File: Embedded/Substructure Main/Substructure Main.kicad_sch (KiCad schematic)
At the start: 30 parts, among them J1 M Pins, J2 C Pins, U1 G0 FFC, U2 G1 FFC, U3 S FFC, U4 USB2513B_Bi, U5 MCP7940N-xMNY, U6 INA220AIDGSR

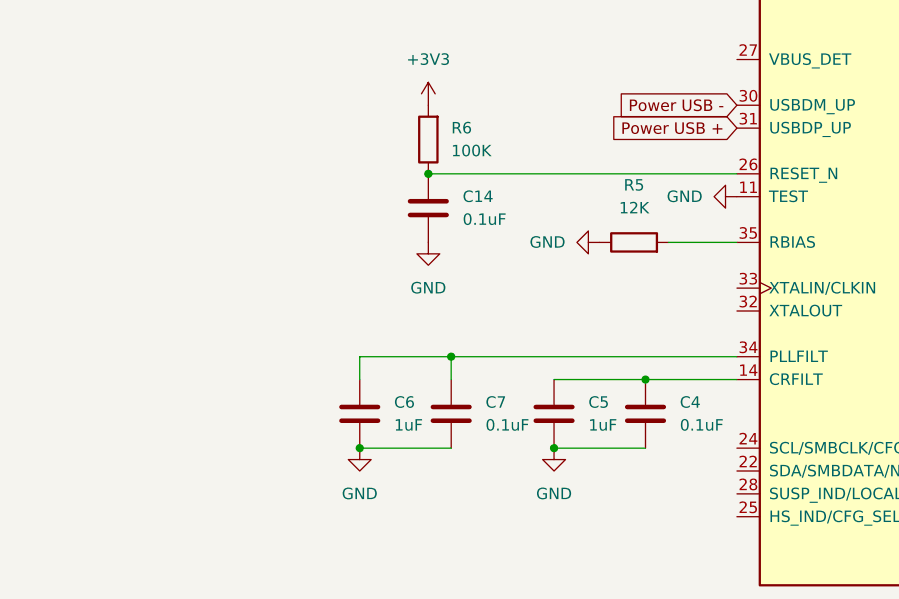
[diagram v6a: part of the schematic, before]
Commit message: Added Crystal to USB2513B_Bi
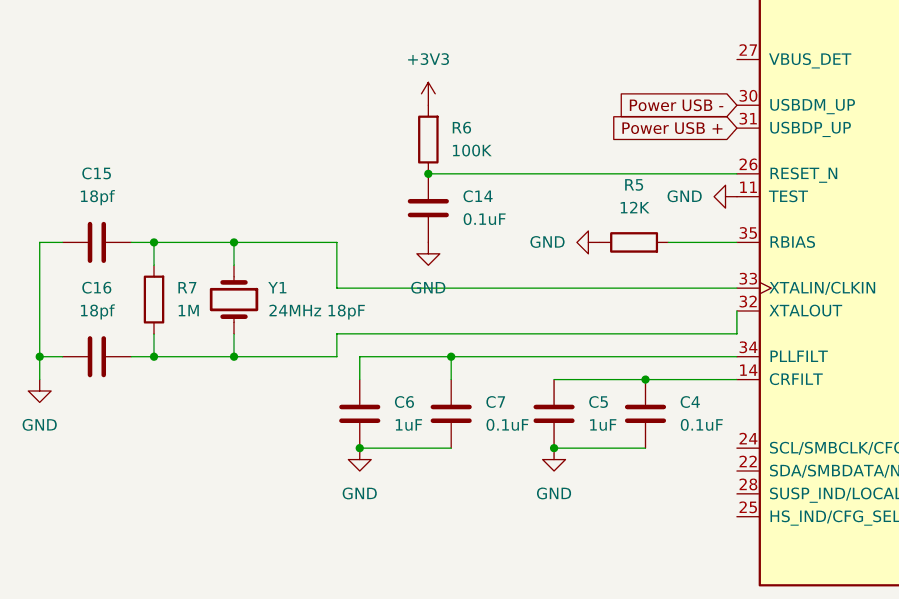
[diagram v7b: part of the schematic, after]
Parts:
- added C15, C16: 18pf, Capacitor_SMD:C_0603_1608Metric_Pad1.08x0.95mm_HandSolder, symbol Device:C
- added R7: 1M, Resistor_SMD:R_0603_1608Metric_Pad0.98x0.95mm_HandSolder, symbol Device:R
- added Y1: 24MHz 18pF, symbol Device:Crystal
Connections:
- net GND: now also C15.1, C16.1
- net at U4.32 (XTALOUT): now also C16.2, R7.1, Y1.2
- net at U4.33 (XTALIN/CLKIN): now also C15.2, R7.2, Y1.1

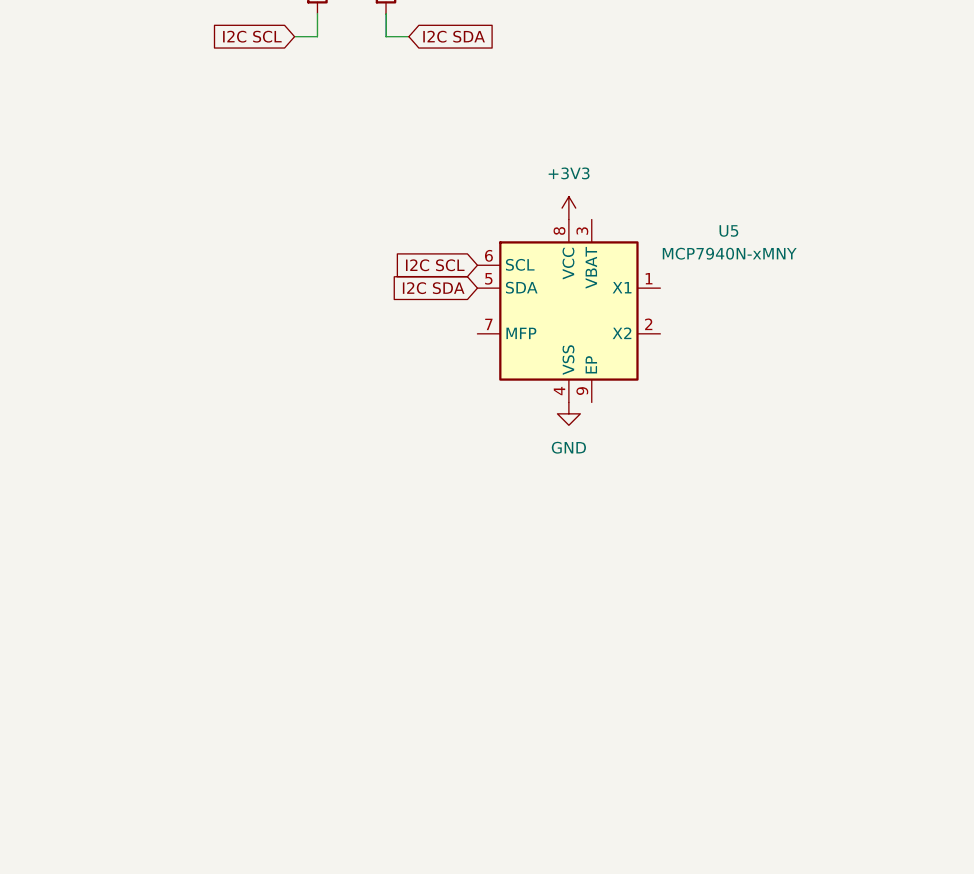
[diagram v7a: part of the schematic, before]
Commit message: Added Crystal & Power to RTC
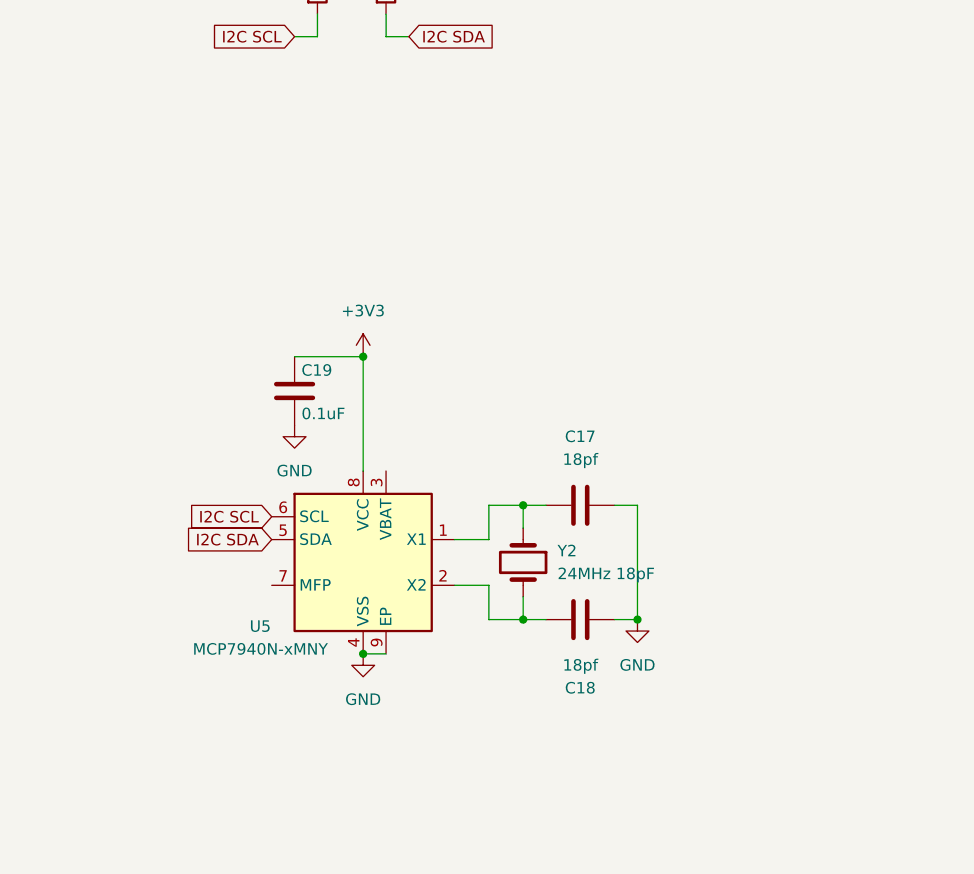
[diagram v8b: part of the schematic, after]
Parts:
- added C17, C18: 18pf, Capacitor_SMD:C_0603_1608Metric_Pad1.08x0.95mm_HandSolder, symbol Device:C
- added C19: 0.1uF, Capacitor_SMD:C_0603_1608Metric_Pad1.08x0.95mm_HandSolder, symbol Device:C
- added Y2: 24MHz 18pF, symbol Device:Crystal
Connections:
- net +3V3: now also C19.1
- net GND: now also U5.9 (EP), C17.2, C18.2, C19.2
- net at U5.1 (X1): now also C17.1, Y2.1
- net at U5.2 (X2): now also C18.1, Y2.2
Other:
- moved on the sheet: U5
